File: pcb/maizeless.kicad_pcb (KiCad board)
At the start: 2 copper layers, 129.8 x 90 mm, 26 parts, among them SW1 SW_PUSH, SW10 SW_PUSH, SW11 SW_PUSH, SW12 SW_PUSH, SW13 SW_PUSH, SW14 SW_PUSH, SW15 SW_PUSH, SW16 SW_PUSH, SW17 SW_PUSH, SW18 SW_PUSH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

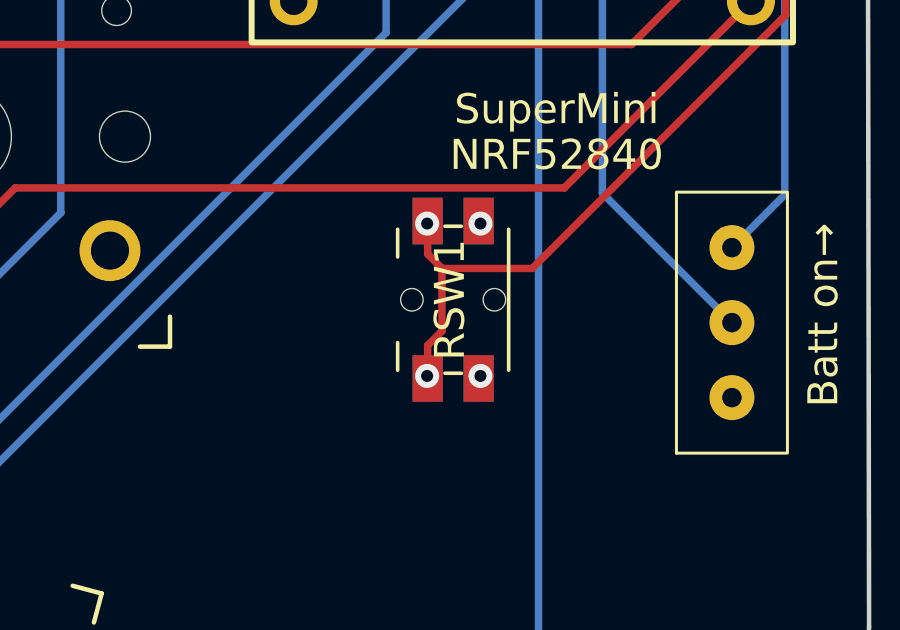
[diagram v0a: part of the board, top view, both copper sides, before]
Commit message: Replace blind vias with thru beside pad
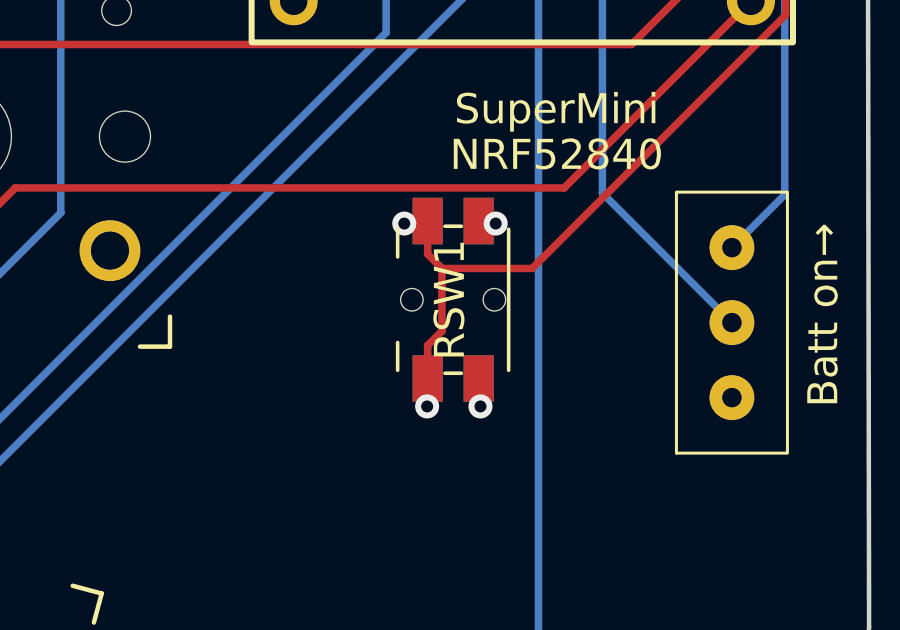
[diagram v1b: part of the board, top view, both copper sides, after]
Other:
- rule pad_to_mask_clearance: 0.2 -> 0
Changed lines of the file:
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@@
       (dielectric_constraints no)
     )
-    (pad_to_mask_clearance 0.2)
-    (solder_mask_min_width 0.1)
+    (pad_to_mask_clearance 0)
     (aux_axis_origin 145.73 12.66)
     (pcbplotparams
@@
       (drillshape 0)
       (scaleselection 1)
-      (outputdirectory "out/gerber/")
+      (outputdirectory "build/")
     )
   )
@@
     (effects (font (size 1 1) (thickness 0.15)))
   )
-  (via blind (at 175.26 103.378) (size 0.8) (drill 0.4) (layers "F.Cu" "B.Cu") (net 1))
-  (via blind (at 175.26 98.298) (size 0.8) (drill 0.4) (layers "F.Cu" "B.Cu") (net 1))
+  (via (at 175.26 104.394) (size 0.8) (drill 0.4) (layers "F.Cu" "B.Cu") (net 1))
+  (via (at 175.768 98.298) (size 0.8) (drill 0.4) (layers "F.Cu" "B.Cu") (net 1))
   (segment (start 175.5527 70.3438) (end 175.5527 71.685) (width 0.25) (layer "F.Cu") (net 3))
   (segment (start 175.5523 70.3434) (end 175.5527 70.3438) (width 0.25) (layer "F.Cu") (net 3))
@@
   (segment (start 173.499 103.463) (end 173.499 102.3611) (width 0.25) (layer "F.Cu") (net 4))
   (segment (start 184.2743 68.0294) (end 185.4341 69.1892) (width 0.25) (layer "F.Cu") (net 4))
-  (via blind (at 173.482 98.298) (size 0.8) (drill 0.4) (layers "F.Cu" "B.Cu") (net 4))
-  (via blind (at 173.482 103.378) (size 0.8) (drill 0.4) (layers "F.Cu" "B.Cu") (net 4))
+  (via (at 172.72 98.298) (size 0.8) (drill 0.4) (layers "F.Cu" "B.Cu") (net 4))
+  (via (at 173.482 104.394) (size 0.8) (drill 0.4) (layers "F.Cu" "B.Cu") (net 4))
   (segment (start 173.499 98.7639) (end 173.499 98.213) (width 0.25) (layer "B.Cu") (net 4))
   (segment (start 185.4033 97.3387) (end 183.642 99.1) (width 0.25) (layer "B.Cu") (net 6))
